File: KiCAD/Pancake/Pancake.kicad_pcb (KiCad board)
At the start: 2 copper layers, 192 parts, among them IC10 LF347N, IC3 LF347N, IC4 LF347N, IC5 LF347N, IC6 LF347N, IC7 LF347N, IC8 LF347N, IC9 LF347N, J1 Conn_01x08_Male, J101 TB001-500-04BE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

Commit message: Thiccccc Traces
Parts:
- moved C101 217.4 mm to (244.3, 50.8)
- moved J102 43.2 mm to (195.6, 32.5)
- moved R101 43.2 mm to (220.5, 32.0)
- moved J101 42.2 mm to (186.4, 31.5)
- moved R19 33.8 mm to (134.1, 142.2)
- moved R1 24.1 mm to (225.6, 111.8)
- moved R10 24.1 mm to (235.7, 91.4)
- moved R15 24.1 mm to (225.6, 76.2)
- moved R16 24.1 mm to (225.6, 96.5)
- moved R17 24.1 mm to (225.6, 86.4)
- moved R21 24.1 mm to (225.6, 66.5)
- moved R23 24.1 mm to (225.6, 81.3)
- moved R4 24.1 mm to (225.6, 106.7)
- moved R6 24.1 mm to (225.6, 116.8)
- moved R9 24.1 mm to (235.7, 71.1)
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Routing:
- net +12V: track 513.6 -> 444.2 mm
- net /ADC1011/IN1: track 321.8 -> 266.5 mm
- net Net-(C101-Pad2): track 0.00 -> 46.0 mm
- net /SPRKPos: track 60.7 -> 102.6 mm
- net /SPRKNeg: track 80.8 -> 122.2 mm
- net Net-(Q901-Pad12): track 69.7 -> 110.8 mm, vias 1 -> 0
- net /VolumeMid: track 136.5 -> 98.2 mm
- net /DriveMid: track 215.4 -> 183.0 mm, vias 0 -> 1
- net /ADC89/IN1: track 234.5 -> 205.8 mm
- net /ToneMid: track 178.8 -> 152.0 mm, vias 0 -> 1
- net /ADC89/IN2: track 246.2 -> 223.4 mm
- net Net-(IC3-Pad8): track 13.6 -> 35.6 mm
- net /DAC01/IN2: track 158.1 -> 137.0 mm
- net Net-(IC3-Pad13): track 7.84 -> 29.0 mm
- net /6VOut: track 20.5 -> 41.0 mm
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
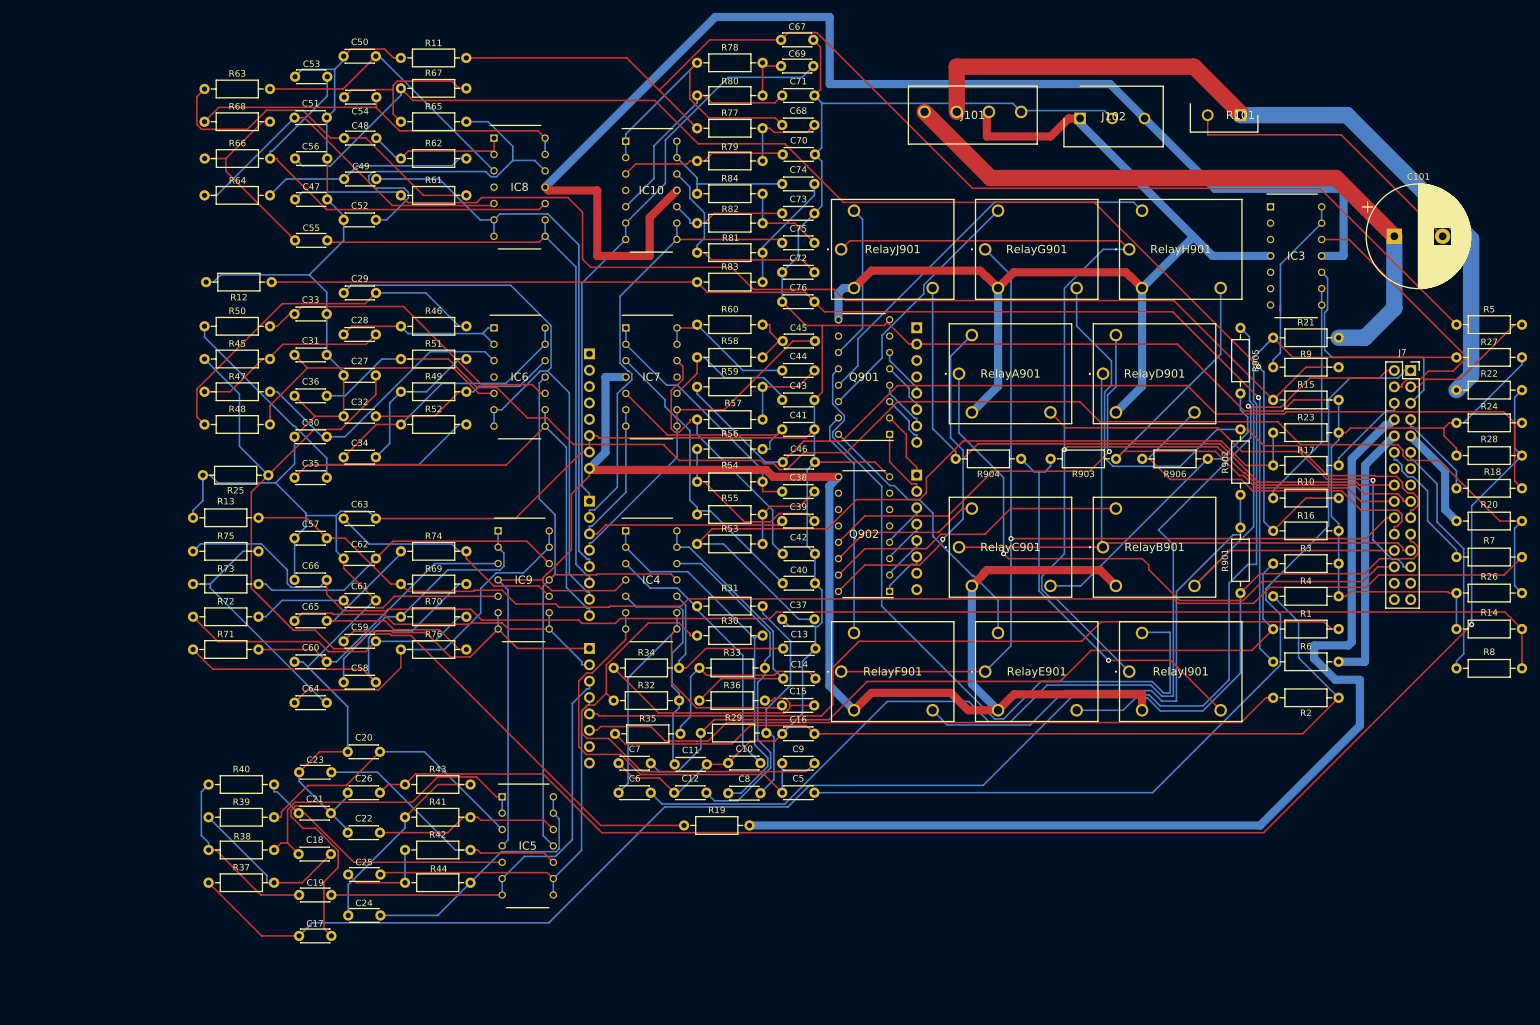
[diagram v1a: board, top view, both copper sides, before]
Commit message: The traces is all that is left. we may fall into problems with mark with clearances, we will see.
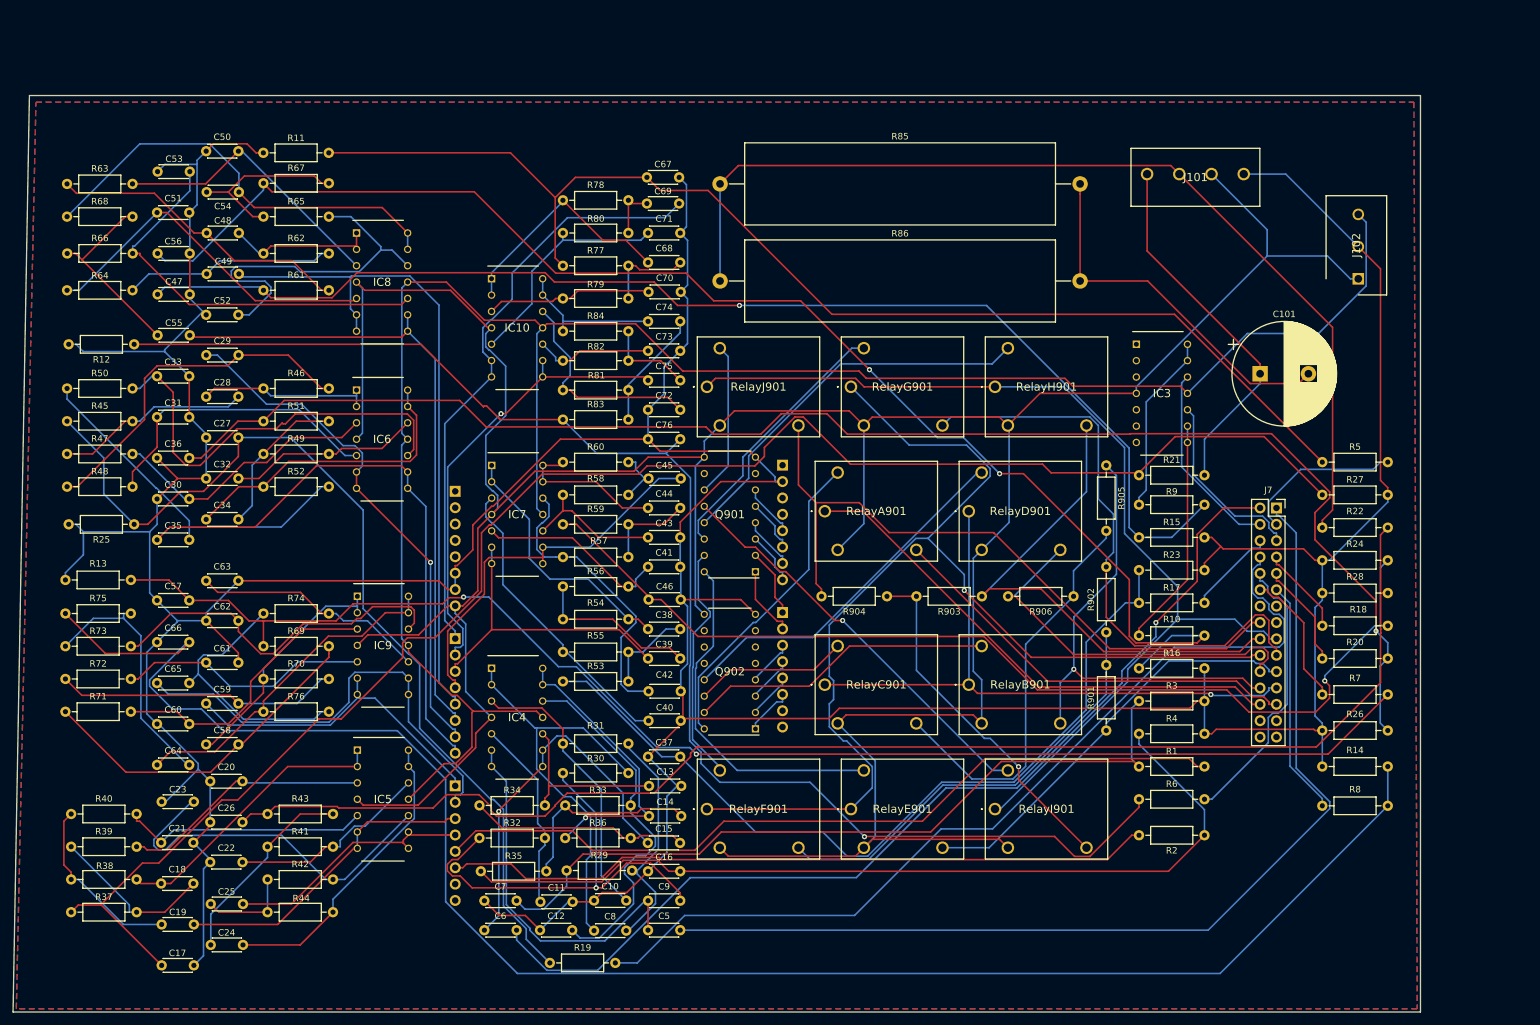
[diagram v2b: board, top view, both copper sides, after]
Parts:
- removed R101: PWR220T-35-8R00F, SamacSys_Parts:TO508P438X1010X1539-2P
- added R85: 10, Resistor_THT:R_Axial_Power_L48.0mm_W12.5mm_P55.88mm, F.Cu at (139.7, 42.7)
- added R86: 10, Resistor_THT:R_Axial_Power_L48.0mm_W12.5mm_P55.88mm, F.Cu at (139.7, 57.7)
- moved J102 49.8 mm to (238.8, 57.4), turned to 90 degrees
- moved J101 35.9 mm to (221.0, 41.1)
- moved R8 29.8 mm to (243.3, 139.2)
- moved R14 29.8 mm to (243.3, 133.1)
- moved R18 29.8 mm to (243.3, 111.3)
- moved R20 29.8 mm to (243.3, 116.3)
- moved R22 29.8 mm to (243.3, 96.0)
- moved R24 29.8 mm to (243.3, 101.1)
- moved R26 29.8 mm to (243.3, 127.5)
- moved R28 29.8 mm to (243.3, 106.2)
- moved R7 29.8 mm to (243.3, 121.9)
- moved C10 29.8 mm to (120.1, 153.9)
- moved C16 29.8 mm to (128.5, 149.4)
- moved C5 29.8 mm to (128.5, 158.5)
- moved C6 29.8 mm to (103.1, 158.5)
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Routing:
- net +12V: track 444.2 -> 527.3 mm
- net /ADC89/IN2: track 223.4 -> 270.7 mm
- net Net-(Q901-Pad12): track 110.8 -> 64.1 mm, vias 0 -> 1
- net /SPRKPos: track 102.6 -> 57.6 mm
- net /SPRKNeg: track 122.2 -> 153.5 mm
- net /ToneMid: track 152.0 -> 179.2 mm
- net /DriveMid: track 183.0 -> 158.4 mm, vias 1 -> 0
- net /ADC11: track 60.5 -> 39.3 mm
- net /12VOut: track 162.4 -> 141.4 mm
- net /ADC10: track 68.4 -> 48.9 mm
- net /ADC01/IN2: track 202.5 -> 221.7 mm
- net /ADC9: track 52.6 -> 71.0 mm
- net /GuitarIn: track 141.5 -> 158.9 mm
- net Net-(C23-Pad1): track 40.2 -> 57.3 mm
- net /PresenceOut: track 97.0 -> 80.0 mm, vias 1 -> 0
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- added copper zone on B.Cu, net GND
- added copper zone on F.Cu, net GND
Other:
- board outline added: 218.4 x 142.2 mm

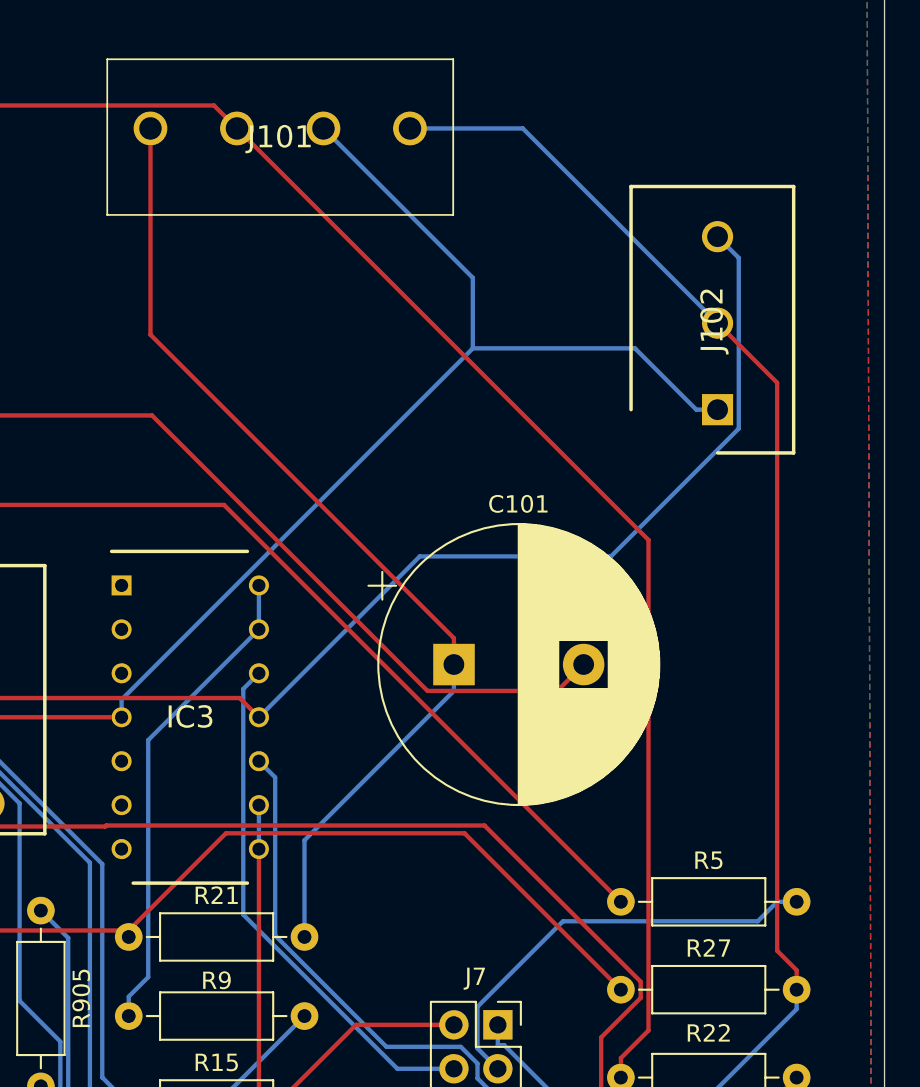
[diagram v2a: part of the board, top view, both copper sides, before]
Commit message: LED for connection of power. I was not able to find the footprint for the 1206 SMD LED that is in the Senior design lab, but I was able to find one for a similar model. With that being said, the model is the same but the specs are different. I believe this shouldn't be a problem as I just needed the Surface mount plates that could hold the LED from the Lab. Will add the Active low LED tomorrow , need to look at what pins I can use for LED and 5V.
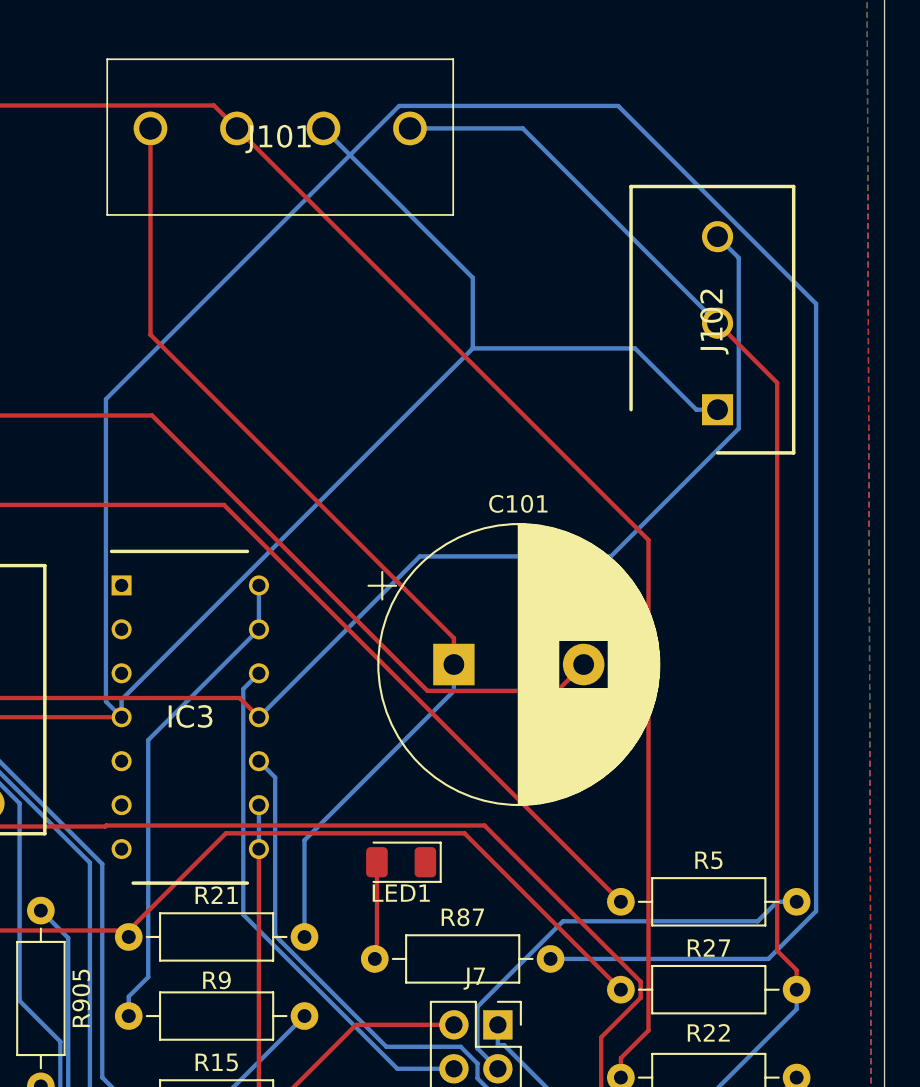
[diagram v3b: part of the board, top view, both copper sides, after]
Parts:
- added LED1: 150120GS75000, LED_SMD:LED_1206_3216Metric, F.Cu at (220.5, 83.6)
- added R87: 500, Resistor_THT:R_Axial_DIN0207_L6.3mm_D2.5mm_P10.16mm_Horizontal, F.Cu at (218.9, 89.2)
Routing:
- net +12V: track 527.3 -> 650.5 mm
- net Net-(LED1-Pad2): track 0.00 -> 5.64 mm

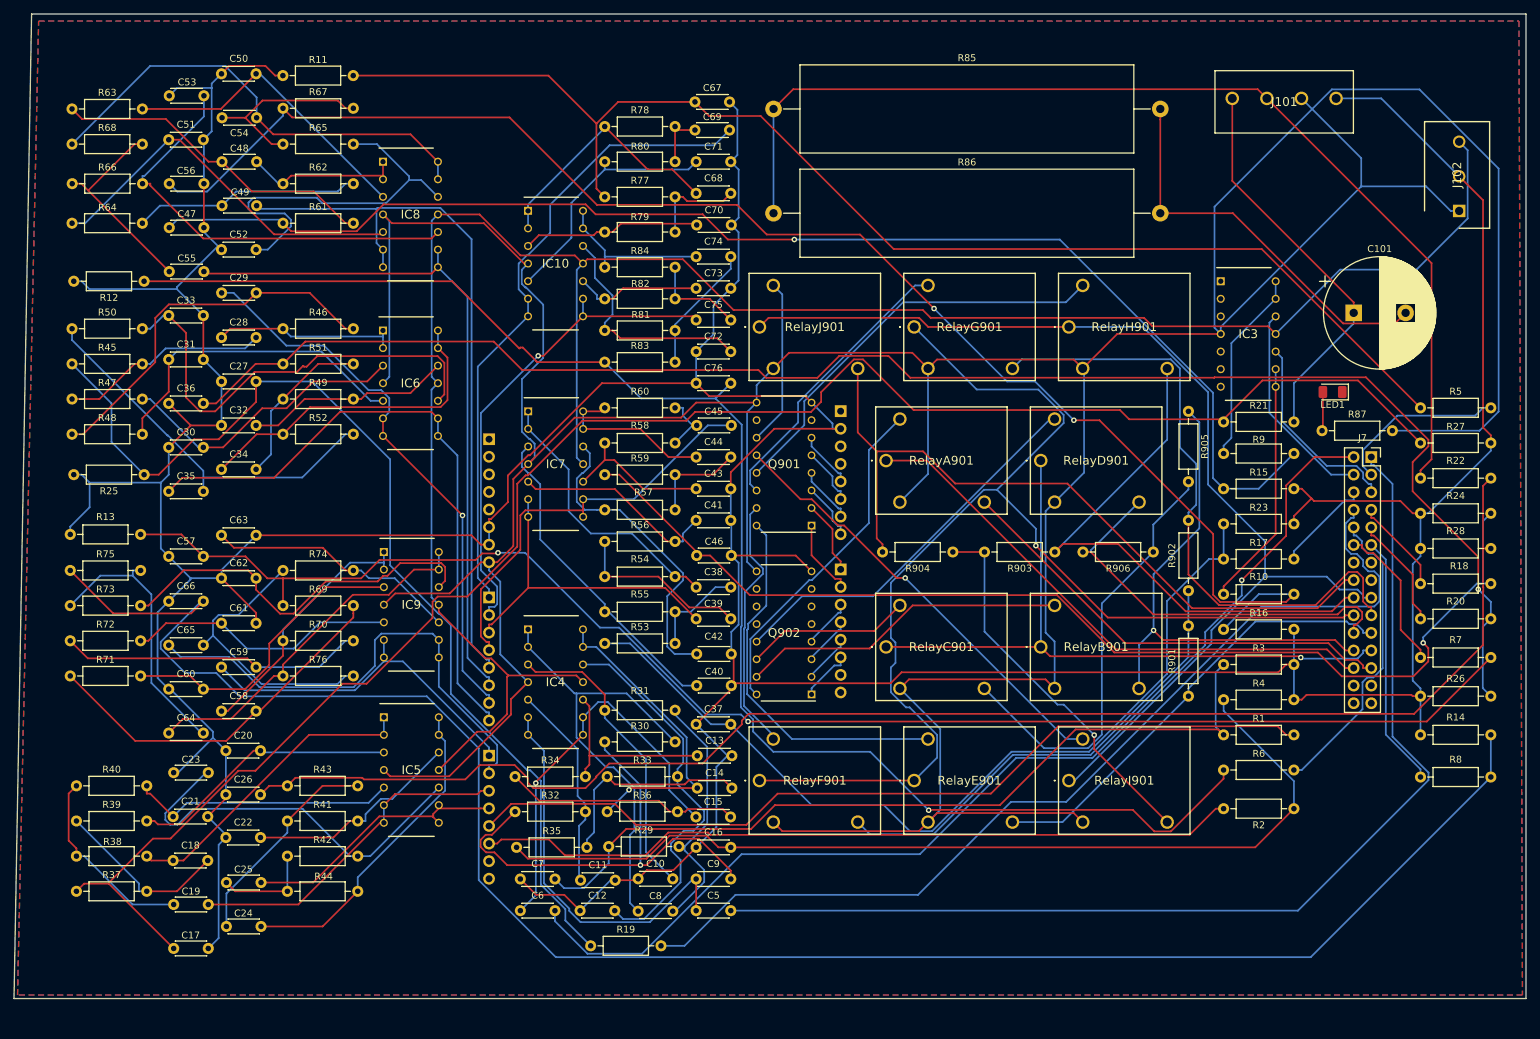
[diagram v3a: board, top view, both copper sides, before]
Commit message: Will need to retrace in order to be built at SDSU.
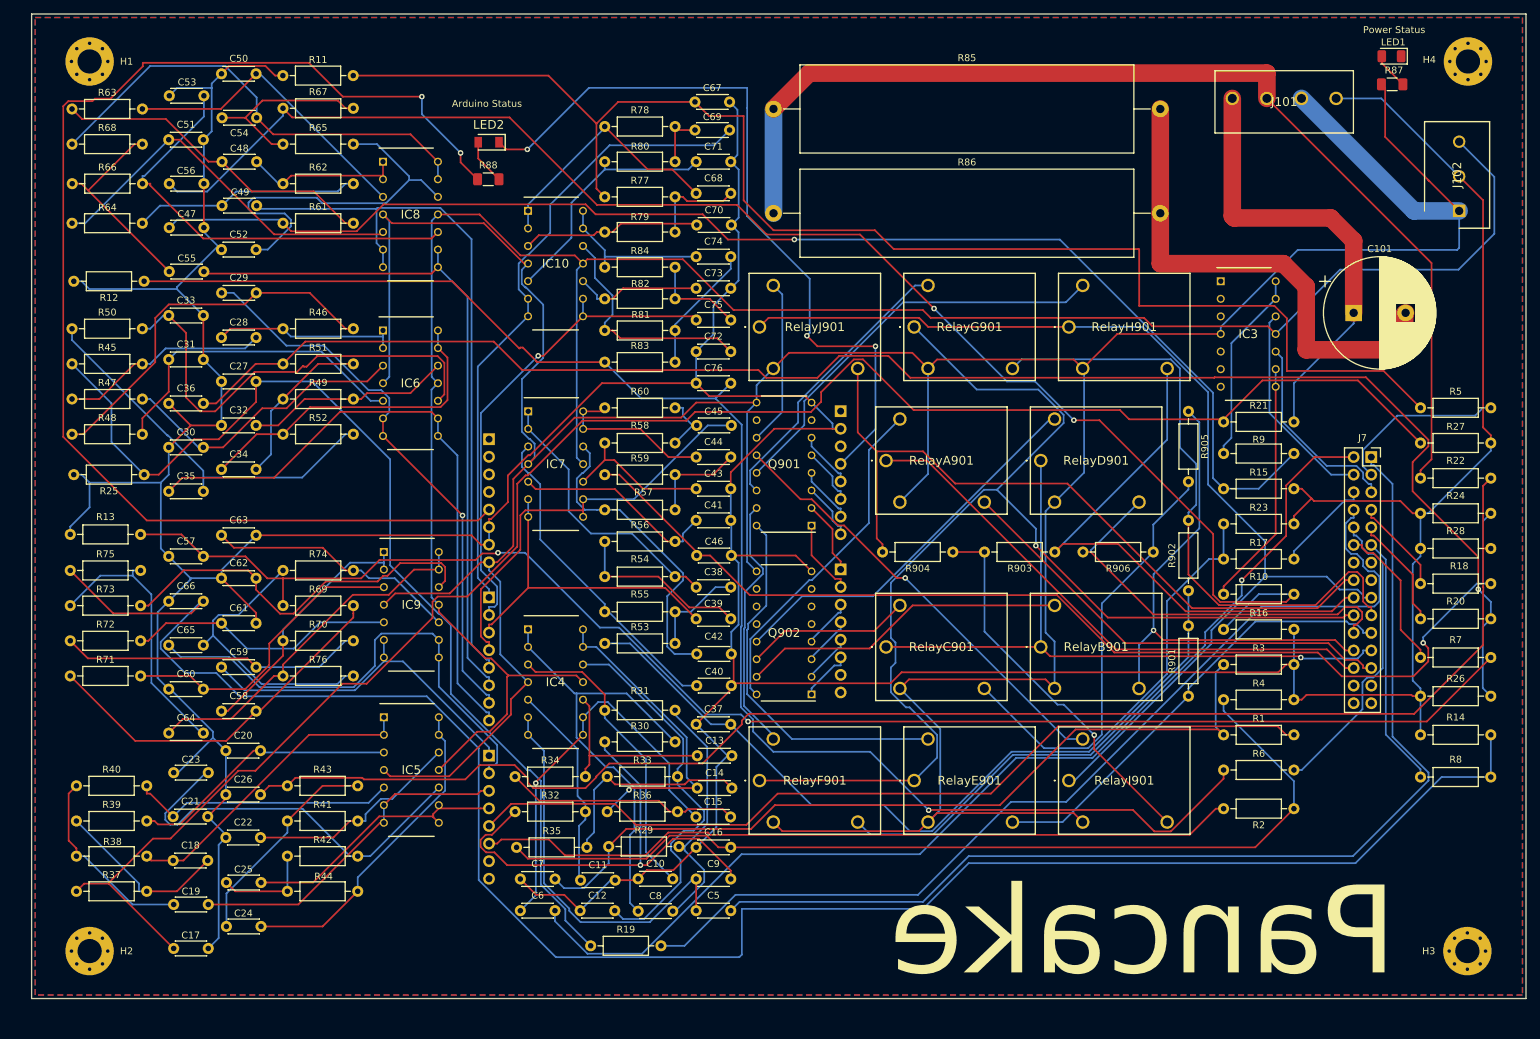
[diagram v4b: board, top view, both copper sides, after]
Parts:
- added H1: MountingHole_Pad, MountingHole:MountingHole_3.5mm_Pad_Via, F.Cu at (40.9, 35.8)
- added H2: MountingHole_Pad, MountingHole:MountingHole_3.5mm_Pad_Via, F.Cu at (40.9, 164.3)
- added H3: MountingHole_Pad, MountingHole:MountingHole_3.5mm_Pad_Via, F.Cu at (239.9, 164.3)
- added H4: MountingHole_Pad, MountingHole:MountingHole_3.5mm_Pad_Via, F.Cu at (240.0, 35.8)
- added LED2: 150120GS75000, SamacSys_Parts:LEDC3214X78N, F.Cu at (98.5, 47.5)
- added R88: 150, Resistor_SMD:R_1206_3216Metric_Pad1.30x1.75mm_HandSolder, F.Cu at (98.5, 52.8)
- R87: footprint Resistor_THT:R_Axial_DIN0207_L6.3mm_D2.5mm_P10.16mm_Horizontal -> Resistor_SMD:R_1206_3216Metric_Pad1.30x1.75mm_HandSolder
- moved R87 51.1 mm to (229.1, 39.1), turned to 180 degrees
- moved LED1 49.3 mm to (229.0, 35.1)
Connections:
- J4 pad 4: Net-(J4-Pad4) -> /D12
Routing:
- net +5V: track 0.00 -> 187.0 mm, vias 0 -> 2
- net /D12: track 0.00 -> 109.3 mm, vias 0 -> 3
- net +12V: track 650.5 -> 563.9 mm
- net /ADC01/IN1: track 187.8 -> 204.1 mm
- net Net-(C101-Pad2): track 57.7 -> 73.6 mm
- net /SPRKPos: track 57.6 -> 65.8 mm
- net -12V: track 307.6 -> 314.7 mm
- net Net-(LED2-Pad2): track 0.00 -> 6.60 mm
- net /SPRKNeg: track 153.5 -> 157.5 mm
- net /ADC89/IN2: track 270.7 -> 274.6 mm
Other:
- board size 218.4 x 142.2 mm -> 215.9 x 142.2 mm
- board text added: "Arduino Status"
- board text added: "Pancake"
- board text added: "Power Status"
